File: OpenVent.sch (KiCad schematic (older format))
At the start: 0 parts

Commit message: Rick added system block diagram to the top level sheet and changed some file names.
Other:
- note added: "+3V3"
- note added: "+3V3-ALWAYS-ON"
- note added: "+5V"
- note added: "+5V_SENSE"
- note added: "12 V\nLimiter"
- note added: "4.65x"
- note added: "50x"
- note added: "BUF"
- note added: "Battery\nCharger"
- note added: "Current\n Sense"
- note added: "Diff Press"
- note added: "Display"
- note added: "FPGA"
- note added: "FTDI\nJTAG"
- note added: "Flow Press"
- note added: "ISNS"
- note added: "JMPR"
- note added: "JTAG"
- note added: "Key Pad"
- note added: "MCU"
- note added: "Motor\nController"
- note added: "O2"
- note added: "PGOOD"
- note added: "Pat Press"
- note added: "STAT2"
- note added: "SWD"
- note added: "UART"
- note added: "USB"
- note added: "USB-JTAG"
- note added: "VBATT-\nSCALED"
- note added: "Vbatt"
- note added: "Vdc"
- note added: "fo"
- note added: "nSTAT1"

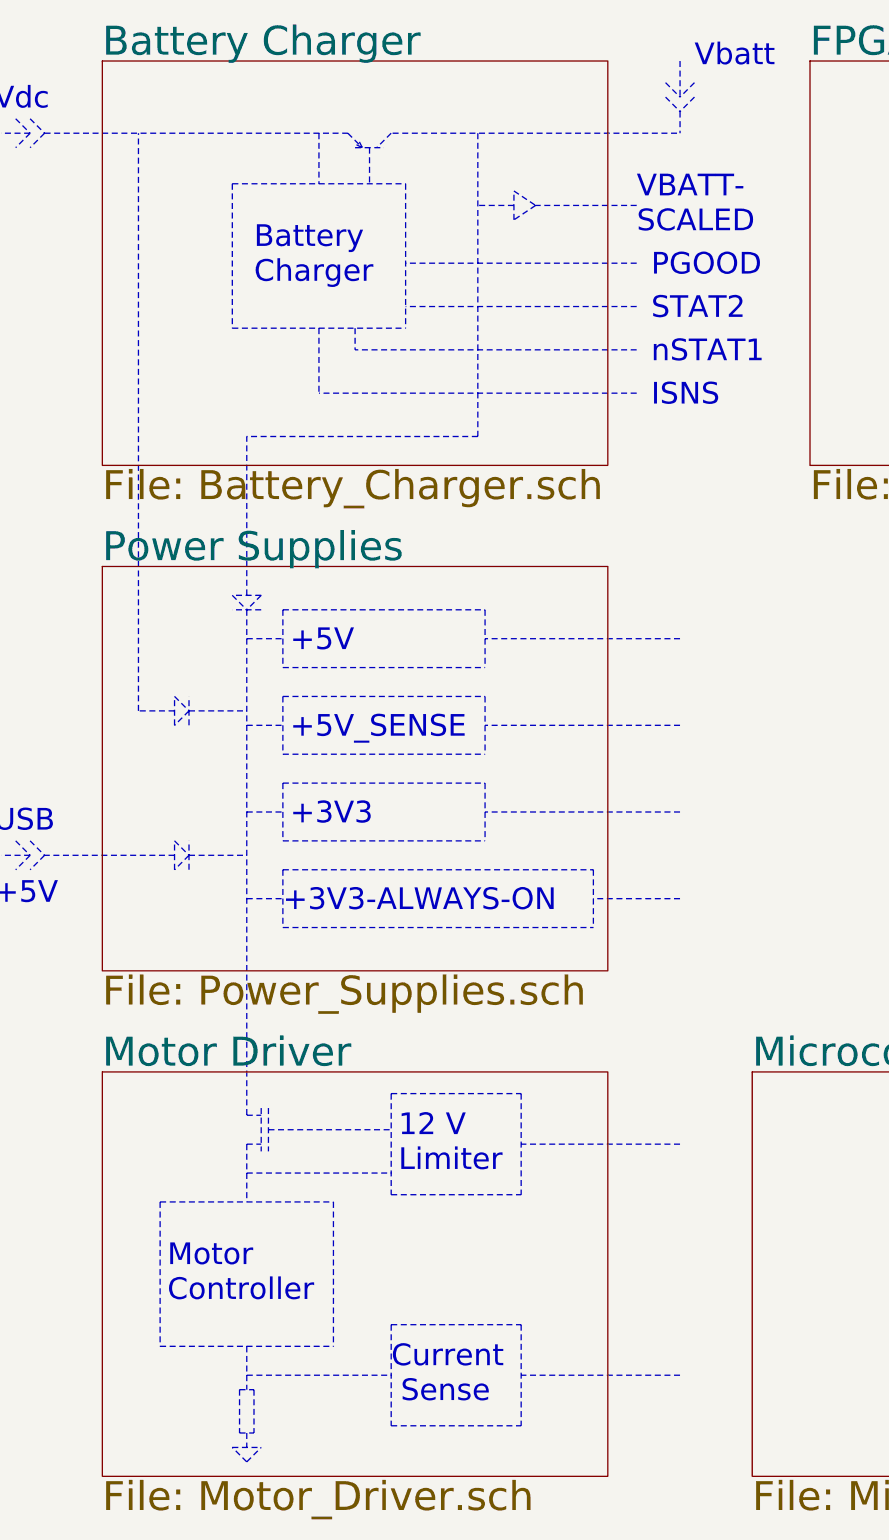
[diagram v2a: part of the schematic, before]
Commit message: Sorted out the interconnect between power supply and main boards.
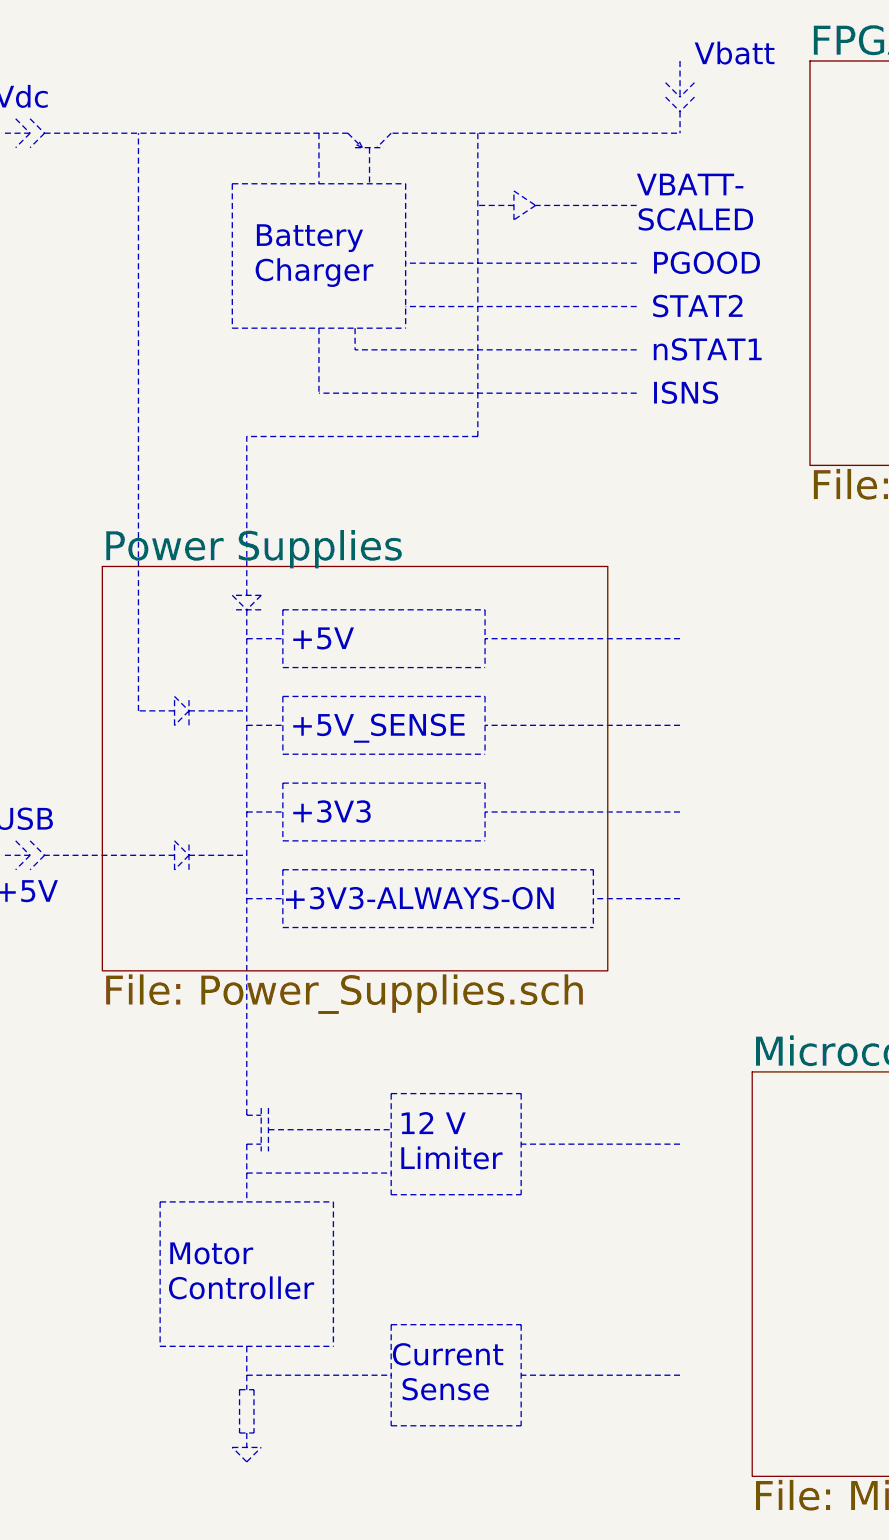
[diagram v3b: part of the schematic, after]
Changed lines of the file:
@@
 $Descr A3 16535 11693
 encoding utf-8
-Sheet 1 8
+Sheet 1 6
 Title "OpenVent Control Board"
 Date "2020-10-20"
@@
 Text Notes 3550 8700 0    150  ~ 0
  12 V\nLimiter
-$Sheet
-S 1500 8000 3500 2800
-U 5F8EE7D2
-F0 "Motor Driver" 200
-F1 "Motor_Driver.sch" 200
-$EndSheet
 Wire Notes Line style solid
 	2500 8700 3500 8700
@@
 Wire Notes Line style solid
 	1100 1500 3200 1500
-$Sheet
-S 1500 1000 3500 2800
-U 5F8F649B
-F0 "Battery Charger" 200
-F1 "Battery_Charger.sch" 200
-$EndSheet
 Wire Notes Line style solid
 	10000 10750 10000 11000

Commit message: Successful merge of Shrookie's changes to main
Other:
- note removed: "12 V\nLimiter"
- note removed: "Battery\nCharger"
- note removed: "Current\n Sense"
- note removed: "ISNS"
- note removed: "Motor\nController"
- note removed: "PGOOD"
- note removed: "STAT2"
- note removed: "VBATT-\nSCALED"
- note removed: "Vdc"
- note removed: "nSTAT1"
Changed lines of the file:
@@
 $Descr A3 16535 11693
 encoding utf-8
-Sheet 1 6
+Sheet 1 8
 Title "OpenVent Control Board"
 Date "2020-10-20"
@@
 MCU
 Wire Notes Line style solid
-	2500 8300 2600 8300
-Wire Notes Line style solid
-	2500 8500 2600 8500
-Wire Notes Line style solid
-	2600 8250 2600 8550
-Wire Notes Line style solid
-	2650 8250 2650 8550
-Wire Notes Line style solid
-	1900 8900 1900 9900
-Wire Notes Line style solid
-	3100 8900 3100 9900
-Wire Notes Line style solid
-	1900 9900 3100 9900
-Wire Notes Line style solid
-	1900 8900 3100 8900
-Wire Notes Line style solid
-	2500 8500 2500 8900
-Wire Notes Line style solid
-	3500 8150 3500 8850
-Wire Notes Line style solid
-	4400 8150 4400 8850
-Wire Notes Line style solid
-	3500 8850 4400 8850
-Wire Notes Line style solid
 	3500 8150 4400 8150
-Wire Notes Line style solid
-	2650 8400 3500 8400
-Text Notes 3550 8700 0    150  ~ 0
- 12 V\nLimiter
-Wire Notes Line style solid
-	2500 8700 3500 8700
-Wire Notes Line style solid
-	3500 9750 3500 10450
-Wire Notes Line style solid
-	4400 9750 4400 10450
-Wire Notes Line style solid
-	3500 10450 4400 10450
-Wire Notes Line style solid
-	3500 9750 4400 9750
-Text Notes 3500 10300 0    150  ~ 0
-Current\n Sense
-Wire Notes Line style solid
-	2500 9900 2500 10200
-Wire Notes Line style solid
-	2500 10100 3500 10100
-Text Notes 1950 9600 0    150  ~ 0
-  Motor\nController
-Wire Notes Line style solid
-	2450 10200 2450 10500
-Wire Notes Line style solid
-	2550 10200 2550 10500
-Wire Notes Line style solid
-	2450 10500 2550 10500
-Wire Notes Line style solid
-	2450 10200 2550 10200
-Wire Notes Line style solid
-	2400 10600 2600 10600
-Wire Notes Line style solid
-	2500 10500 2500 10600
-Wire Notes Line style solid
-	2500 10700 2600 10600
-Wire Notes Line style solid
-	2500 10700 2400 10600
-Wire Notes Line style solid
-	2400 1850 2400 2850
-Wire Notes Line style solid
-	3600 1850 3600 2850
-Wire Notes Line style solid
-	2400 1850 3600 1850
-Wire Notes Line style solid
-	3000 1500 3000 1850
-Text Notes 2550 2550 0    150  ~ 0
-Battery\nCharger
-Wire Notes Line style solid
-	1750 5500 1750 1500
-Wire Notes Line style solid
-	1100 1500 1000 1600
-Wire Notes Line style solid
-	1000 1400 1100 1500
-Wire Notes Line style solid
-	1000 1500 900  1600
-Wire Notes Line style solid
-	900  1400 1000 1500
-Wire Notes Line style solid
-	1000 1500 800  1500
-Text Notes 750  1350 0    150  ~ 0
-Vdc
 Text Notes 750  6350 0    150  ~ 0
 USB
@@
 Wire Notes Line style solid
 	2600 4700 2400 4700
-Wire Notes Line style solid
-	2500 4700 2500 3600
-Wire Notes Line style solid
-	2500 4800 2500 8300
-Wire Notes Line style solid
-	4100 3600 2500 3600
-Wire Notes Line style solid
-	5500 1350 5500 1500
-Wire Notes Line style solid
-	5600 1250 5500 1350
-Wire Notes Line style solid
-	5400 1250 5500 1350
-Wire Notes Line style solid
-	5600 1150 5500 1250
-Wire Notes Line style solid
-	5400 1150 5500 1250
-Wire Notes Line style solid
-	5500 1000 5500 1250
 Text Notes 5600 1050 0    150  ~ 0
 Vbatt
-Wire Notes Line style solid
-	4500 2000 4350 2100
-Wire Notes Line style solid
-	4350 1900 4500 2000
-Wire Notes Line style solid
-	4350 2100 4350 1900
-Wire Notes Line style solid
-	4350 2000 4100 2000
-Wire Notes Line style solid
-	5200 2000 4500 2000
-Text Notes 5200 2200 0    150  ~ 0
-VBATT-\nSCALED
-Text Notes 5300 2500 0    150  ~ 0
-PGOOD
-Wire Notes Line style solid
-	5200 2400 3600 2400
-Text Notes 5300 2800 0    150  ~ 0
-STAT2
-Text Notes 5300 3100 0    150  ~ 0
-nSTAT1
-Wire Notes Line style solid
-	4100 1500 4100 3600
-Text Notes 5300 3400 0    150  ~ 0
-ISNS
-Wire Notes Line style solid
-	2400 2850 3600 2850
-Wire Notes Line style solid
-	5200 2700 3600 2700
-Wire Notes Line style solid
-	5200 3000 3250 3000
-Wire Notes Line style solid
-	5200 3300 3000 3300
-Wire Notes Line style solid
-	3250 2850 3250 3000
 Wire Notes Line style solid
 	2750 4800 2750 5200
@@
 	5500 6800 4900 6800
 Wire Notes Line style solid
-	5500 8500 4400 8500
-Wire Notes Line style solid
-	5500 10100 4400 10100
-Wire Notes Line style solid
 	2100 6500 2500 6500
 Wire Notes Line style solid
@@
 $EndSheet
 Wire Notes Line style solid
-	3200 1500 3300 1600
-Wire Notes Line style solid
-	3500 1500 3400 1600
-Wire Notes Line style solid
-	3250 1600 3450 1600
-Wire Notes Line style solid
-	3350 1600 3350 1850
-Wire Notes Line style solid
-	3280 1560 3300 1600
-Wire Notes Line style solid
-	3260 1580 3300 1600
-Wire Notes Line style solid
-	3510 1500 5500 1500
-Wire Notes Line style solid
-	1100 1500 3200 1500
-Wire Notes Line style solid
 	10000 10750 10000 11000
 Text Notes 10050 11100 0    150  ~ 0
@@
 Wire Notes Line style solid
 	10900 9750 10900 10650
-Wire Notes Line style solid
-	3000 2850 3000 3300
 Wire Notes Line style solid
 	15600 1400 15500 1500
@@
 Text Notes 11350 7850 0    150  ~ 0
 JMPR
+$Sheet
+S 1500 1050 3500 850
+U 5FBE832C
+F0 "FPGA JTAG SPECIAL" 50
+F1 "FPGA_JTAG_SPECIAL.sch" 50
+$EndSheet
+$Sheet
+S 1500 2400 3500 850
+U 5FBE8499
+F0 "FPGA JTAG SPECIAL PWR" 50
+F1 "FPGA_JTAG_SPECIAL_PWR.sch" 50
+$EndSheet
 $EndSCHEMATC

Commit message: Stuff
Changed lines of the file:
@@
 JMPR
 $Sheet
-S 1500 1050 3500 850
-U 5FBE832C
-F0 "FPGA JTAG SPECIAL" 50
-F1 "FPGA_JTAG_SPECIAL.sch" 50
-$EndSheet
-$Sheet
-S 1500 2400 3500 850
+S 1475 1075 3500 850
 U 5FBE8499
 F0 "FPGA JTAG SPECIAL PWR" 50
 F1 "FPGA_JTAG_SPECIAL_PWR.sch" 50
 $EndSheet
+$Sheet
+S 1500 2175 3500 550
+U 5FCA4074
+F0 "Buzzer_LEDs" 50
+F1 "Buzzer_LEDs.sch" 50
+$EndSheet
 $EndSCHEMATC

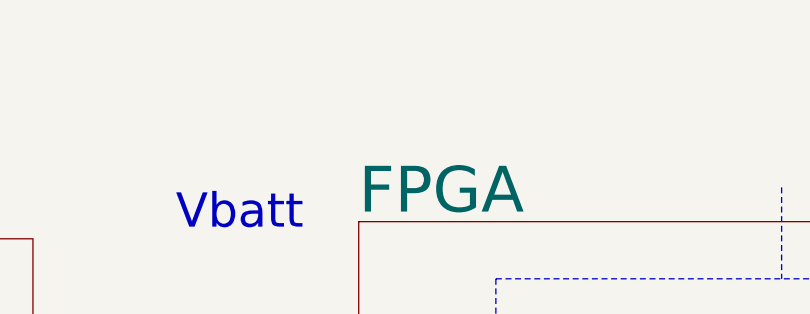
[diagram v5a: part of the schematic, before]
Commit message: Went through the Task list with Darren 1:1 with Ebony, possible new volunteer Changed gain on MPX4006DP to 8.5 gain Added a second MPXV4006GP Took sensor data off MCU: Pressure sensor (patient), oxygen sensor, flow sensor gain, flow sensor to be on FPGA only. Left alerts, battery sensor, and current measurements on MCU. Added circuit for Sensiron SM3020 and scaled output to 3v3.
Went through the Task list with Darren
1:1 with Ebony, possible new volunteer
Changed gain on MPX4006DP to 8.5 gain
Added a second MPXV4006GP
Took sensor data off MCU: Pressure sensor (patient), oxygen sensor, flow sensor gain, flow sensor to be on FPGA only. Left alerts, battery sensor, and current measurements on MCU.
Added circuit for Sensiron SM3020 and scaled output to 3v3.
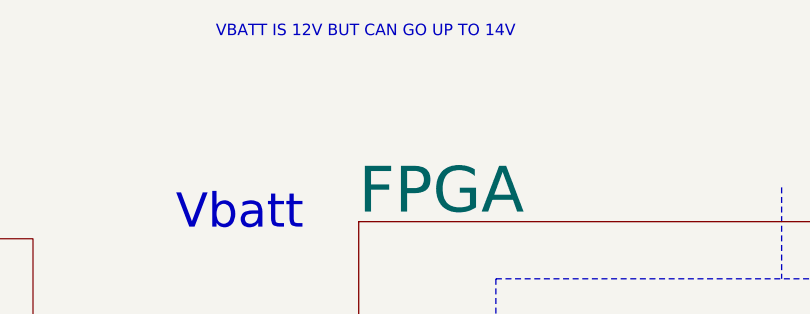
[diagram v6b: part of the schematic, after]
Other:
- note added: "VBATT IS 12V BUT CAN GO UP TO 14V"
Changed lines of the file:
@@
 F1 "Buzzer_LEDs.sch" 50
 $EndSheet
+Text Notes 5775 200  0    50   ~ 0
+VBATT IS 12V BUT CAN GO UP TO 14V
 $EndSCHEMATC

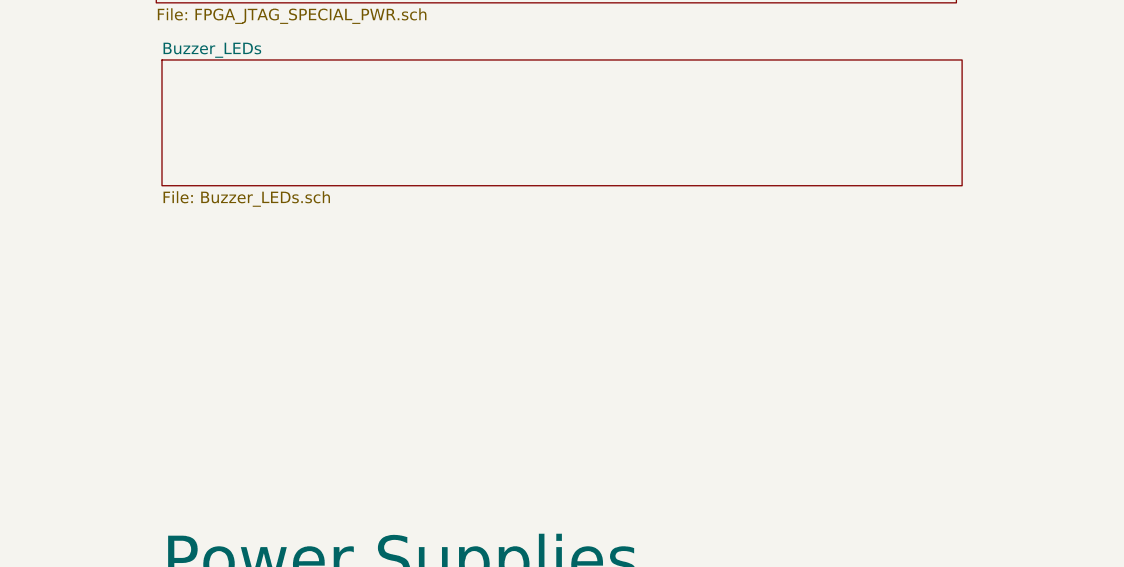
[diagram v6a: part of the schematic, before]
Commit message: Minor cleanup on power supply board.  Added Sigma Delta circuitry for A/D conversion by the FPGA, just need pin assignments for all of the signals.
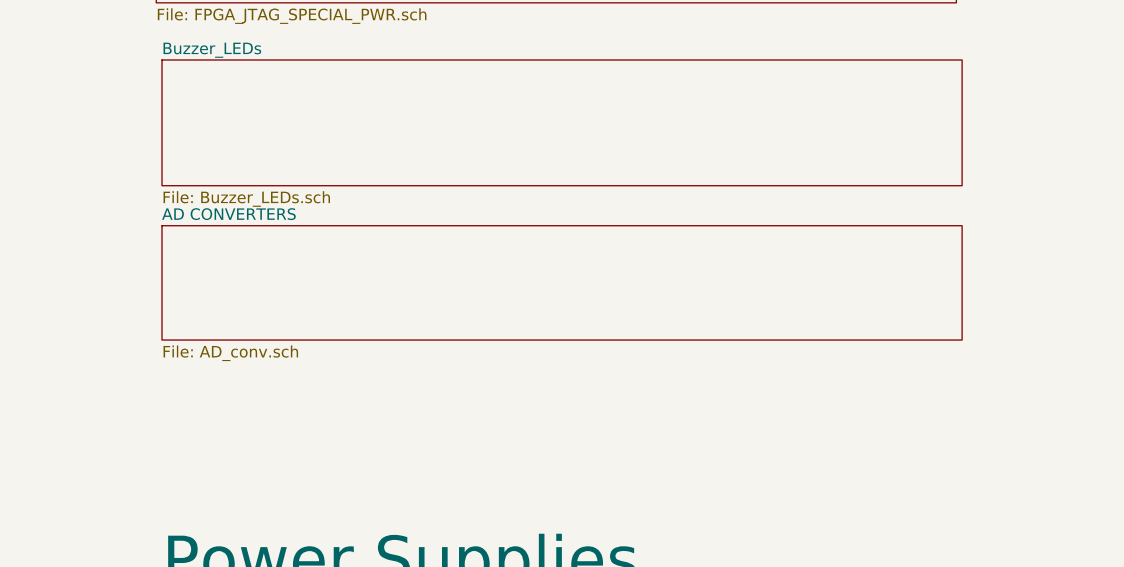
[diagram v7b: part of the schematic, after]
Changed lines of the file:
@@
 $Descr A3 16535 11693
 encoding utf-8
-Sheet 1 8
+Sheet 1 9
 Title "OpenVent Control Board"
 Date "2020-10-20"
@@
 Text Notes 5775 200  0    50   ~ 0
 VBATT IS 12V BUT CAN GO UP TO 14V
+$Sheet
+S 1500 2900 3500 500
+U 601B7AF8
+F0 "AD CONVERTERS" 50
+F1 "AD_conv.sch" 50
+$EndSheet
 $EndSCHEMATC
